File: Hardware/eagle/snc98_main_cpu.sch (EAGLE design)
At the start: 151 parts, among them IC1 MCP170333MB, M1 IRLML2244, M10 IRLML2244, M11 IRLML2244, M12 IRLML2244, M2 IRLML2244, M3 IRLML2244, M4 IRLML2244, M5 IRLML2244, M6 IRLML2244, M7 IRLML2244, M8 IRLML2244, M9 IRLML2244, U1 74HC4051_MUX, U3 ATMEGA1284P-PU, U4 TLV70033, X1 MICROMATCH-12, X3 MICROMATCH-12, Y2 12MHz

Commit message: snc98_main_cpu V1.0
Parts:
- removed BH4, BH5: HOLDER_AAA_LEFT1, SparkFun-Electromechanical:HOLDER_AAA_LEFT1
- removed BH6: HOLDER_AAA_RIGHT, SparkFun-Electromechanical:HOLDER_AAA_RIGHT
- removed D14, D15, D16, D17, D18, D19, D2, D20, D21, D22, D23, D24, D25, D26, D27: SC40-11_UNISC40-11_UNI, display-hp:SC40-11_UNISC40-11_UNI
- removed JP1, JP4: RXD_1, adafruit:PINHD-1X1CB
- removed JP10, JP11, JP12, JP7, JP8, JP9: (no value), adafruit:PINHD-1X1
- removed JP2: TXD_1, adafruit:PINHD-1X1CB
- removed KP1, KP2: KEYPAD, KeyPad3x4:KEYPAD
- removed LOGO2: OSHW_LOGO_6MILX0100-NT, ohw-logo:OSHW_LOGO_6MILX0100-NT
- removed M10, M11, M4, M5, M6, M7, M8, M9: IRLML2244, IRLML6402:IRLML6402
- removed R10, R11, R12, R13, R14, R15, R16, R17, R18, R19, R5, R6, R7, R8, R9: 22, rcl:R-EU_R1210
- removed R26: 6k8, rcl:R-EU_0204/5
- removed R29, R54, R55, R56, R57, R58, R59: 3k3, rcl:R-EU_0204/5
- removed R30: 3V3, rcl:R-EU_0204/5
- removed R36, R37, R38, R39, R40, R41, R42, R43: 3k3, rcl:R-EU_R1206
- removed X1, X3: MICROMATCH-12, Con-amp-micromatch:MICROMATCH-12
- added C13: 100n, rcl:C-EUC1206K
- added JP15: (no value), adafruit:PINHD-1X9
- added JP3: (no value), adafruit:PINHD-1X8CLEANBIG
- C1, C2, C3, C6: device _jc:C-US025_050-025X075 -> _jc:C-USC1206K
- C14, C15, C18, C4, C9: device rcl:C-EU025_050-025X075 -> rcl:C-EUC1206K
- C7, C8: device _jc:C-US025-024X044 -> _jc:C-USC0805K
- R1, R21, R22, R25, R28, R31, R32, R33, R34, R35, R4, R44, R46, R47, R48, R50, R51: device rcl:R-EU_0204/7 -> rcl:R-EU_R1206
- R2: value 6k8 -> 56R
- R20: device rcl:R-EU_0204/5 -> rcl:R-EU_R1206
- U$2: device transistor-power:IRLML2502 -> transistor-power:IRLML2502M
- U$3: value HT7333 -> HT7333 / TS9011SCY
- U4: value TLV70033 -> TLV70033 / TC1185
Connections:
- removed net CA_LED: M10.S, M11.S, M4.S, M5.S, M6.S, M7.S, M8.S, M9.S, R29.1, R30.1, R36.1, R37.1, R38.1, R39.1, R40.1, R41.1, R42.1, R43.1, R54.1, R55.1, R56.1, R57.1, R58.1, R59.1, X3-8.S
- removed net D0_A: R5.2, X3-1.S
- removed net D10_A: R15.2, X1-8.S
- removed net D11_A: R16.2, X1-9.S
- removed net D12_A: R17.2, X1-10.S
- removed net D13_A: R18.2, X1-11.S
- removed net D14_A: R19.2, X1-12.S
- removed net D1_A: R6.2, X3-2.S
- removed net D2_A: R7.2, X3-3.S
- removed net D3_A: R8.2, X3-4.S
- removed net D4_A: R9.2, X3-5.S
- removed net D5_A: R10.2, X3-6.S
- removed net D6_A: R11.2, X3-7.S
- removed net D7_A: R12.2, X1-5.S
- removed net D8_A: R13.2, X1-6.S
- removed net D9_A: R14.2, X1-7.S
- removed net DIG_0: D2.CC1, D2.CC2, D2.CC3, D2.CC4, R5.1
- removed net DIG_1: D14.CC1, D14.CC2, D14.CC3, D14.CC4, R6.1
- removed net DIG_10: D23.CC1, D23.CC2, D23.CC3, D23.CC4, R15.1
- removed net DIG_11: D24.CC1, D24.CC2, D24.CC3, D24.CC4, R16.1
- removed net DIG_12: D25.CC1, D25.CC2, D25.CC3, D25.CC4, R17.1
- removed net DIG_13: D26.CC1, D26.CC2, D26.CC3, D26.CC4, R18.1
- removed net DIG_14: D27.CC1, D27.CC2, D27.CC3, D27.CC4, R19.1
- removed net DIG_2: D15.CC1, D15.CC2, D15.CC3, D15.CC4, R7.1
- removed net DIG_3: D16.CC1, D16.CC2, D16.CC3, D16.CC4, R8.1
- removed net DIG_4: D17.CC1, D17.CC2, D17.CC3, D17.CC4, R9.1
- removed net DIG_5: D18.CC1, D18.CC2, D18.CC3, D18.CC4, R10.1
- removed net DIG_6: D19.CC1, D19.CC2, D19.CC3, D19.CC4, R11.1
- removed net DIG_7: D20.CC1, D20.CC2, D20.CC3, D20.CC4, R12.1
- removed net DIG_8: D21.CC1, D21.CC2, D21.CC3, D21.CC4, R13.1
- removed net DIG_9: D22.CC1, D22.CC2, D22.CC3, D22.CC4, R14.1
- removed net GND1: C22.2
- removed net IO-A: M4.G, R29.2, R36.2, X1-4.S
- removed net IO-B: M5.G, R30.2, R37.2, X1-3.S
- removed net IO-C: M6.G, R42.2, R54.2, X1-2.S
- removed net IO-D: M7.G, R38.2, R55.2, X1-1.S
- removed net IO-DP: M11.G, R41.2, R59.2, X3-9.S
- removed net IO-E: M8.G, R43.2, R56.2, X3-12.S
- removed net IO-F: M9.G, R39.2, R57.2, X3-11.S
- removed net IO-G: M10.G, R40.2, R58.2, X3-10.S
- removed net N$2: U$2.S
- removed net NC1: BH4.+, BH7.+
- removed net NC2: BH5.+
- removed net NC3: BH6.-
- removed net SEG_A: D14.A, D15.A, D16.A, D17.A, D18.A, D19.A, D2.A, D20.A, D21.A, D22.A, D23.A, D24.A, D25.A, D26.A, D27.A, M4.D
- removed net SEG_B: D14.B, D15.B, D16.B, D17.B, D18.B, D19.B, D2.B, D20.B, D21.B, D22.B, D23.B, D24.B, D25.B, D26.B, D27.B, M5.D
- removed net SEG_C: D14.C, D15.C, D16.C, D17.C, D18.C, D19.C, D2.C, D20.C, D21.C, D22.C, D23.C, D24.C, D25.C, D26.C, D27.C, JP10.1, JP11.1, JP8.1, M6.D
- removed net SEG_D: D14.D, D15.D, D16.D, D17.D, D18.D, D19.D, D2.D, D20.D, D21.D, D22.D, D23.D, D24.D, D25.D, D26.D, D27.D, M7.D
- removed net SEG_DP: D14.DP, D14.DP1, D15.DP, D15.DP1, D16.DP, D16.DP1, D17.DP, D17.DP1, D18.DP, D18.DP1, D19.DP, D19.DP1, D2.DP, D2.DP1, D20.DP, D20.DP1, D21.DP, D21.DP1, D22.DP, D22.DP1, D23.DP, D23.DP1, D24.DP, D24.DP1, D25.DP, D25.DP1, D26.DP, D26.DP1, D27.DP, D27.DP1, JP12.1, JP7.1, JP9.1, M11.D
- removed net SEG_E: D14.E, D15.E, D16.E, D17.E, D18.E, D19.E, D2.E, D20.E, D21.E, D22.E, D23.E, D24.E, D25.E, D26.E, D27.E, M8.D
- removed net SEG_F: D14.F, D15.F, D16.F, D17.F, D18.F, D19.F, D2.F, D20.F, D21.F, D22.F, D23.F, D24.F, D25.F, D26.F, D27.F, M9.D
- removed net SEG_G: D14.G, D14.G1, D15.G, D15.G1, D16.G, D16.G1, D17.G, D17.G1, D18.G, D18.G1, D19.G, D19.G1, D2.G, D2.G1, D20.G, D20.G1, D21.G, D21.G1, D22.G, D22.G1, D23.G, D23.G1, D24.G, D24.G1, D25.G, D25.G1, D26.G, D26.G1, D27.G, D27.G1, M10.D
- net A4: no longer JP4.1
- net A5: now also JP15.8, JP3.8; no longer KP1.C2, KP2.C2
- net A6: now also JP15.7, JP3.7; no longer KP1.C1, KP2.C1
- net A7: now also JP15.6, JP3.6; no longer KP1.C0, KP2.C0
- net A9: no longer R26.2
- net AREF: now also JP15.9
- net D10_: no longer JP1.1
- net D11_: no longer JP2.1
- net EN: no longer R2.2, R26.1
- net GND: now also U$2.S; no longer R2.1, S3.5
- net GND-ISO: now also C13.1, JP15.1, JP3.1
- net IO_A: now also JP15.5; no longer KP2.R0
- net IO_B: now also JP15.4; no longer KP2.R1
- net IO_C: now also JP15.3; no longer KP2.R2
- net IO_D: now also JP15.2; no longer KP2.R3
- net IO_DP: now also JP3.2; no longer KP1.R3
- net IO_E: now also JP3.5; no longer KP1.R0
- net IO_F: now also JP3.4; no longer KP1.R1
- net IO_G: now also JP3.3; no longer KP1.R2
- net N$1: now also C22.2
- net N$13: now also R2.2
- net N$6: now also R25.2
- net VIN_P: now also R2.1
- net V_IN: now also BH7.+, C13.2, S3.5, U$3.VIN
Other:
- note added: "HT7333-A / TS9011SCY"
- note removed: "HT7333-A"

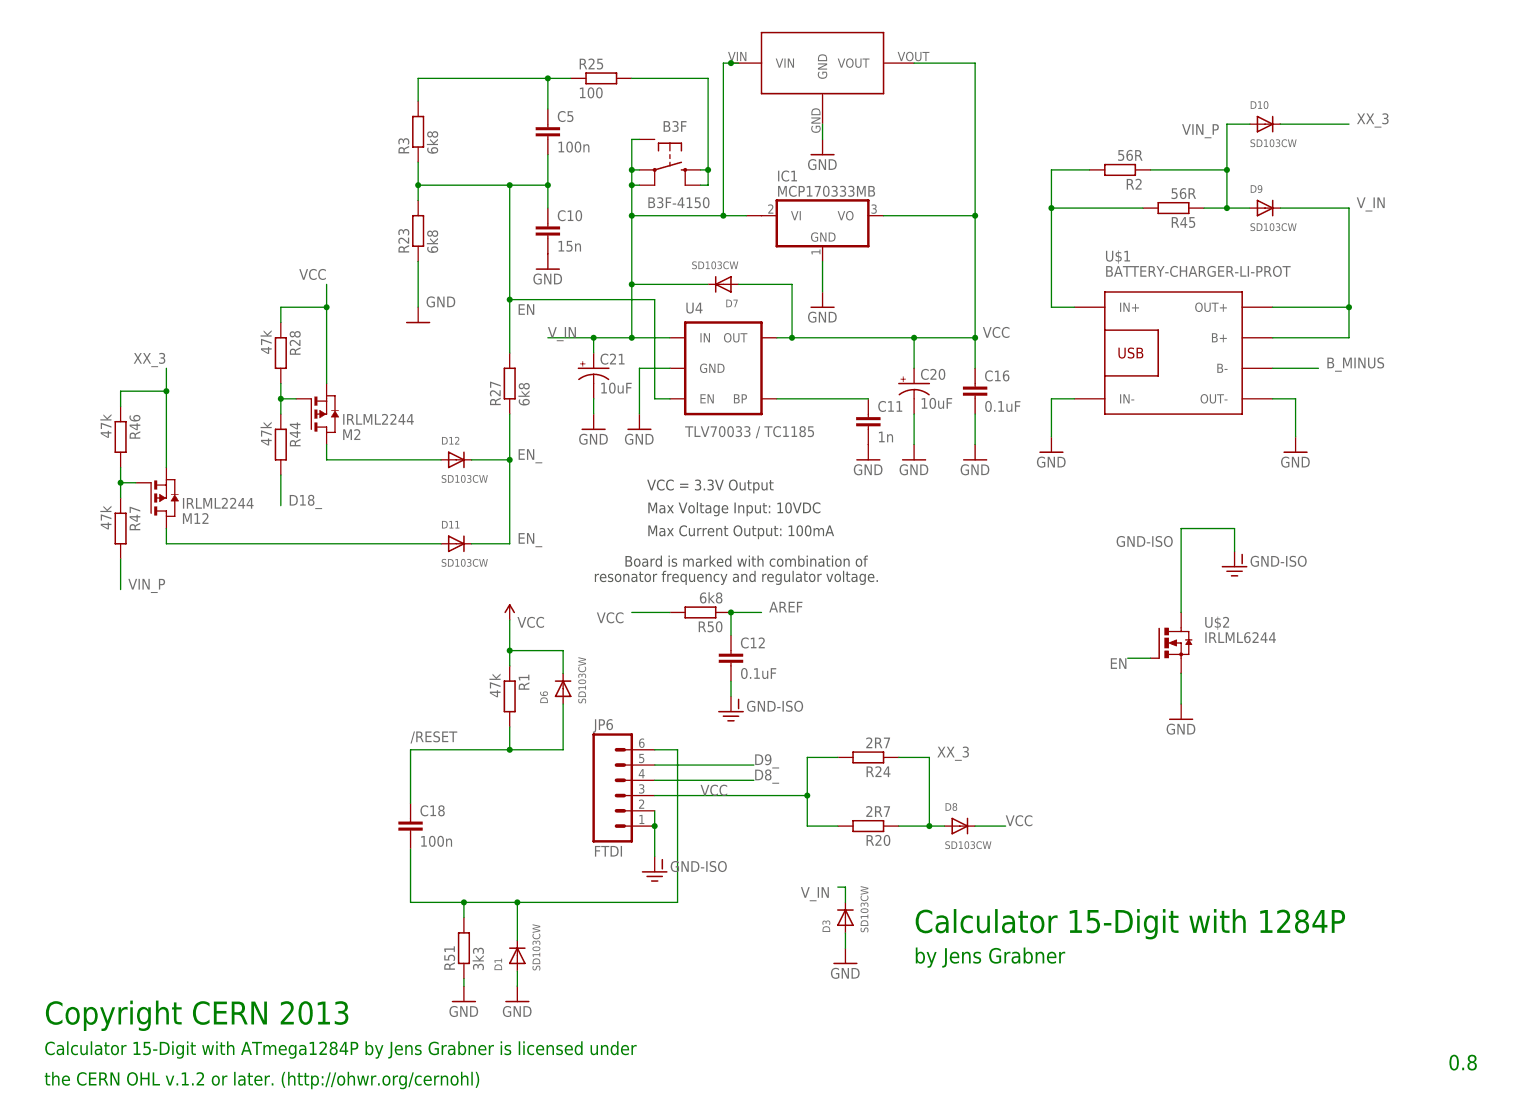
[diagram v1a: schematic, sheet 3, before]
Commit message: new Reset on Main:cpu
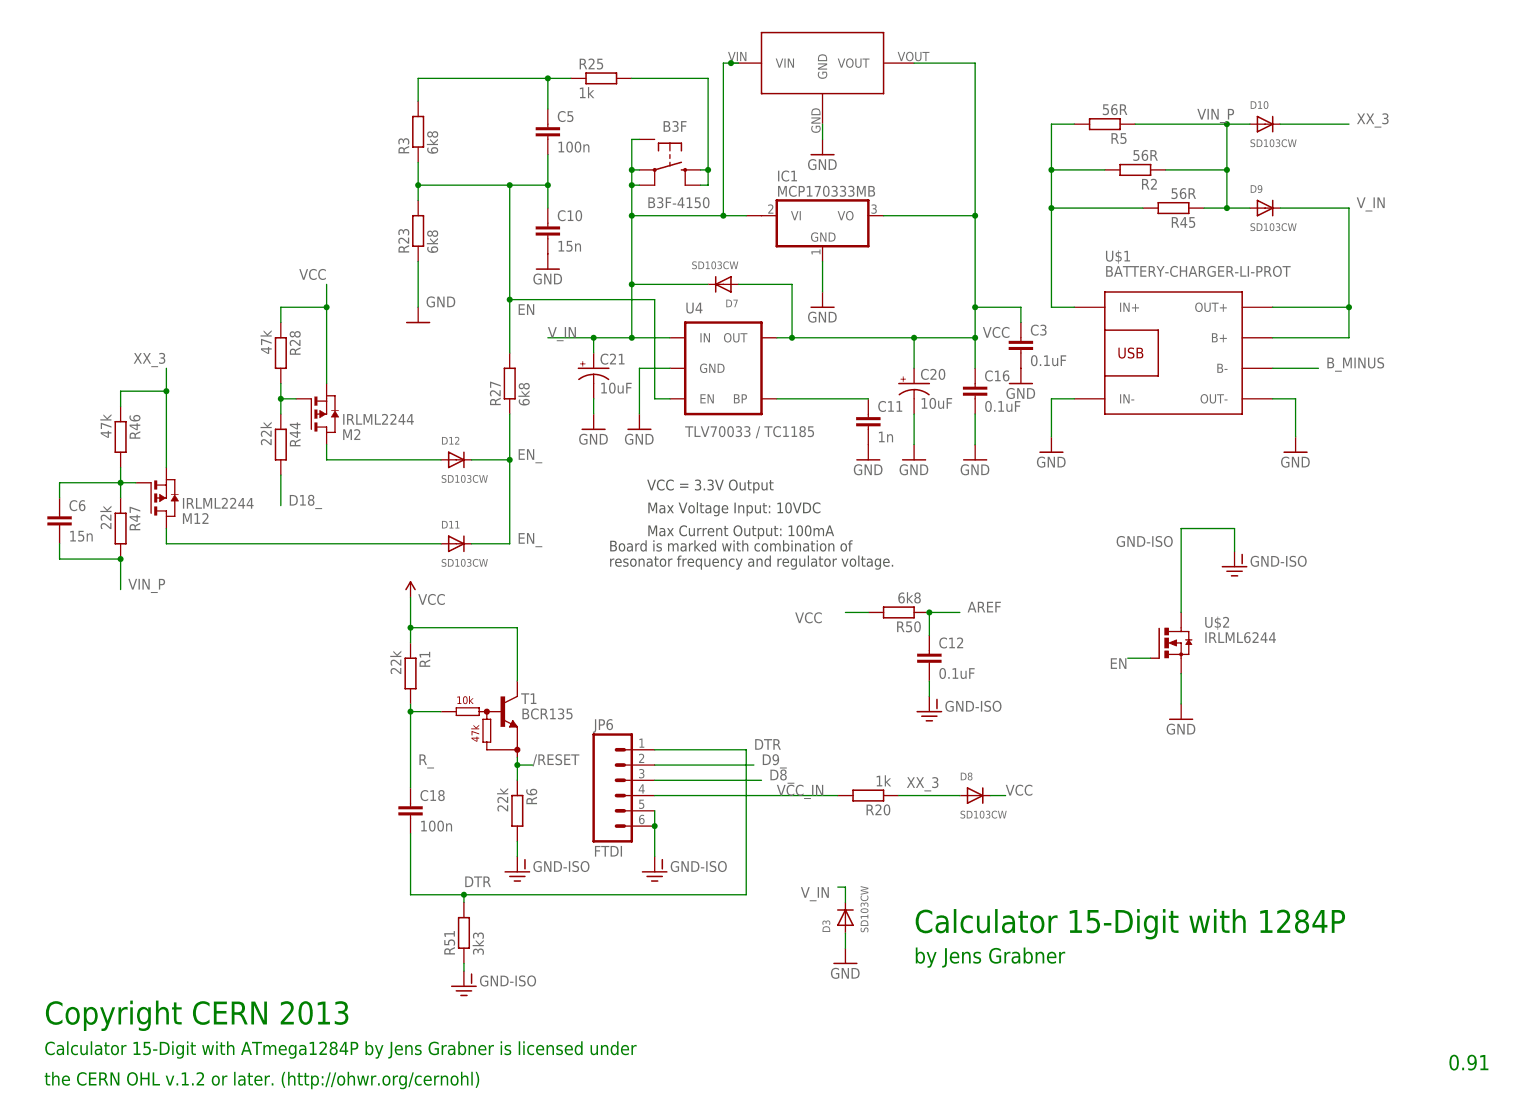
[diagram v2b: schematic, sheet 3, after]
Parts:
- removed D1, D6: SD103CW, BaseApp:DIODESMA
- removed R24: 2R7, rcl:R-EU_R1206
- added R5: 56R, rcl:R-EU_0207/10
- added R6: 22k, rcl:R-EU_R1206
- added T1: BCR135, digital-transistors:BCR135
- C3: value 100nF -> 0.1uF; device _jc:C-USC1206K -> SparkFun:CAP0805
- C6: value 10uF -> 15n; device _jc:C-USC1206K -> rcl:C-EUC1206K
- R1, R44, R47: value 47k -> 22k
- R20: value 2R7 -> 1k
- R25: value 100 -> 1k
- R31, R32: value 100 -> 150
- R33: value 1k -> 6k8
- SG1: value BUZZERNS -> SBT1205-3
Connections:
- removed net N$12: C18.2, D1.C, JP6.6, R51.2
- new net DTR: C18.2, JP6.6, R51.2
- new net R_: C18.1, R1.2, T1.B
- new net VCC_IN: JP6.3, R20.2
- net /RESET: now also R6.1, T1.E; no longer C18.1, D6.A, R1.2
- net GND: now also C3.2; no longer D1.A, R51.1
- net GND-ISO: now also R51.1, R6.2; no longer C3.2, C6.2
- net N$13: now also R5.2
- net N$9: now also C6.1
- net VCC: now also T1.C; no longer C6.1, D6.C, JP6.3, R20.2, R24.2
- net VIN_P: now also C6.2, R5.1
- net XX_3: no longer R24.1
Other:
- note added: "0.91"
- note removed: "0.8"
- moved on the sheet: C12, C18, D8, R1, R2, R20, R50, R51

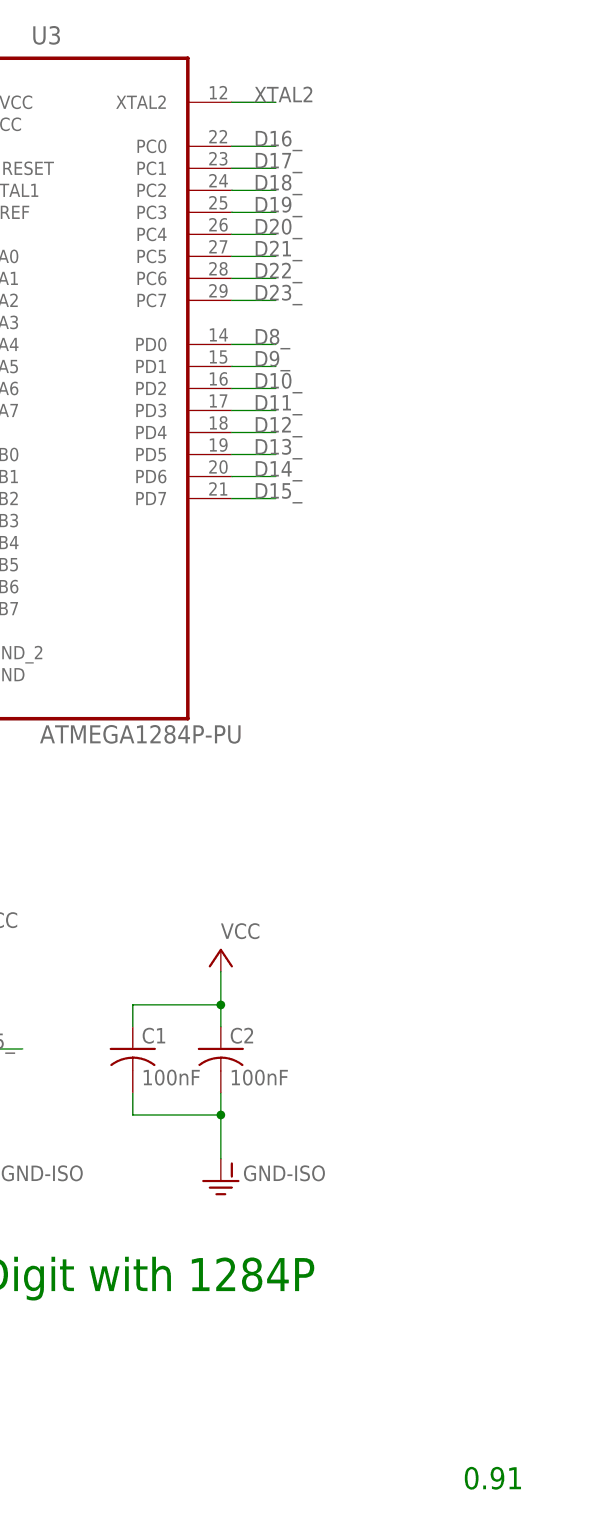
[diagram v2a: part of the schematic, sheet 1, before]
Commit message: Main_cpu_rev_0.95 - Add Onewire DS18B20
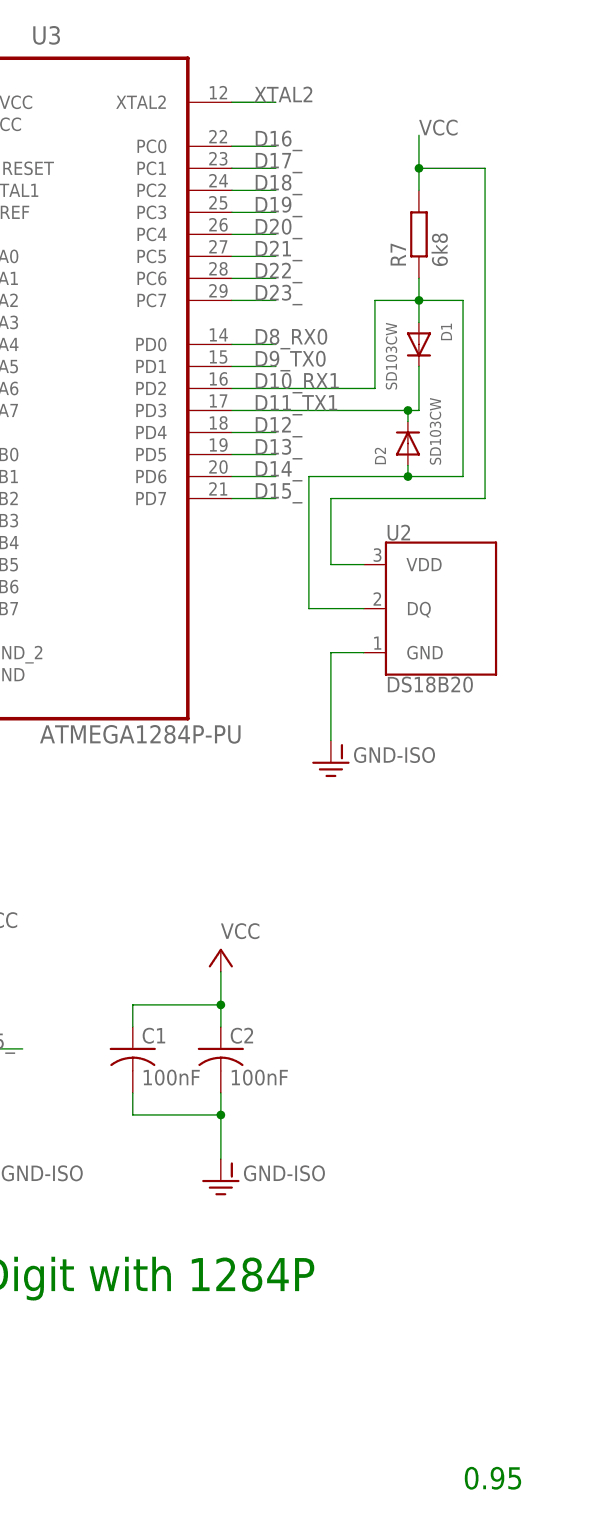
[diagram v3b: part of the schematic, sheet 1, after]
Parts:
- added D1: SD103CW, BaseApp:DIODESOD-323
- added D2: SD103CW, BaseApp:DIODESOD-123
- added R7: 6k8, rcl:R-EU_R1206
- added U2: DS18B20, SparkFun-Sensors:DS18B20
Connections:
- net D8_ renamed D8_RX0
- net D9_ renamed D9_TX0
- removed net D10_: JP13.10, U3.PD2
- removed net D11_: JP13.8, U3.PD3
- new net D10_RX1: D1.A, D2.A, R7.1, U2.DQ, U3.PD2
- new net D11_TX1: D1.C, D2.C, U3.PD3
- net D2_: now also JP13.10
- net D4_: now also JP13.8
- net GND-ISO: now also U2.GND
- net VCC: now also R7.2, U2.VDD
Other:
- note added: "0.95"
- note removed: "0.91"

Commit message: fine with 2 numbers
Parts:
- C1: value 100nF -> 220nF
- C12: value 0.1uF -> 47n
- C13, C5: value 100n -> 47n
- C16, C3: value 0.1uF -> 220nF
- C18: value 100n -> 220n

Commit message: Add new Function: mod (modular)
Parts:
- added T2: BCR135, digital-transistors:BCR135
- added T3: BCR185, digital-transistors-1(1):BCR185
- R2, R45, R5: value 56R -> 150R
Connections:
- removed net AREF: C12.1, JP15.9, M1.S, R50.1, U3.AREF
- new net AREF_+1V: C12.1, JP15.9, M1.S, R50.1, T3.B, U3.AREF
- new net N$2: T1.E, T3.E
- net /RESET: now also T3.C; no longer T1.E
- net VCC: now also T2.E
- net V_IN: now also T2.B, T2.C
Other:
- moved on the sheet: C11, C16, C20, C21, C3, C6, D11, D12, D9, M12, M2, R1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
